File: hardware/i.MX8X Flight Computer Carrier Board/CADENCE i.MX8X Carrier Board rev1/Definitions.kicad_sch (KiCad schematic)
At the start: 8 parts, among them U41 TXS0101DCKR, U42 TXS0101DCKR, U45 TXS0108EPW

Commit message: schematic push
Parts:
- renumbered R159 to R160, R160 to R161, R163 to R162, U41 to U40, U42 to U41, U45 to U42
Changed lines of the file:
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@@
 		(on_board yes)
 		(dnp no)
-		(property "Reference" "#PWR0269"
+		(property "Reference" "#PWR0259"
 			(at 237.49 26.67 0)
 			(effects
@@
 			(project "CADENCE i.MX8X Carrier Board rev1"
 				(path "/de284495-d382-47cb-b528-76e440980d40/f5f49c98-aaea-4f03-a1b3-a277d1d06600/b523867a-62fb-4a81-ab53-06050067b1aa"
-					(reference "#PWR0269")
+					(reference "#PWR0259")
 					(unit 1)
 				)
@@
 		(on_board yes)
 		(dnp no)
-		(property "Reference" "#PWR0259"
+		(property "Reference" "#PWR0255"
 			(at 80.01 52.07 0)
 			(effects
@@
 			(project "CADENCE i.MX8X Carrier Board rev1"
 				(path "/de284495-d382-47cb-b528-76e440980d40/f5f49c98-aaea-4f03-a1b3-a277d1d06600/b523867a-62fb-4a81-ab53-06050067b1aa"
-					(reference "#PWR0259")
+					(reference "#PWR0255")
 					(unit 1)
 				)
@@
 		(on_board yes)
 		(dnp no)
-		(property "Reference" "#PWR0255"
+		(property "Reference" "#PWR0251"
 			(at 44.45 43.18 0)
 			(effects
@@
 			(project "CADENCE i.MX8X Carrier Board rev1"
 				(path "/de284495-d382-47cb-b528-76e440980d40/f5f49c98-aaea-4f03-a1b3-a277d1d06600/b523867a-62fb-4a81-ab53-06050067b1aa"
-					(reference "#PWR0255")
+					(reference "#PWR0251")
 					(unit 1)
 				)
@@
 		(on_board yes)
 		(dnp no)
-		(property "Reference" "#PWR0256"
+		(property "Reference" "#PWR0252"
 			(at 45.72 21.59 0)
 			(effects
@@
 			(project "CADENCE i.MX8X Carrier Board rev1"
 				(path "/de284495-d382-47cb-b528-76e440980d40/f5f49c98-aaea-4f03-a1b3-a277d1d06600/b523867a-62fb-4a81-ab53-06050067b1aa"
-					(reference "#PWR0256")
+					(reference "#PWR0252")
 					(unit 1)
 				)
@@
 		(on_board yes)
 		(dnp no)
-		(property "Reference" "#PWR0260"
+		(property "Reference" "#PWR0256"
 			(at 81.28 33.02 0)
 			(effects
@@
 			(project "CADENCE i.MX8X Carrier Board rev1"
 				(path "/de284495-d382-47cb-b528-76e440980d40/f5f49c98-aaea-4f03-a1b3-a277d1d06600/b523867a-62fb-4a81-ab53-06050067b1aa"
-					(reference "#PWR0260")
+					(reference "#PWR0256")
 					(unit 1)
 				)
@@
 		(on_board yes)
 		(dnp no)
-		(property "Reference" "#PWR0267"
+		(property "Reference" "#PWR0257"
 			(at 232.41 26.67 0)
 			(effects
@@
 			(project "CADENCE i.MX8X Carrier Board rev1"
 				(path "/de284495-d382-47cb-b528-76e440980d40/f5f49c98-aaea-4f03-a1b3-a277d1d06600/b523867a-62fb-4a81-ab53-06050067b1aa"
-					(reference "#PWR0267")
+					(reference "#PWR0257")
 					(unit 1)
 				)
@@
 		(on_board yes)
 		(dnp no)
-		(property "Reference" "R159"
+		(property "Reference" "R160"
 			(at 48.26 44.45 0)
 			(effects
@@
 			(project "CADENCE i.MX8X Carrier Board rev1"
 				(path "/de284495-d382-47cb-b528-76e440980d40/f5f49c98-aaea-4f03-a1b3-a277d1d06600/b523867a-62fb-4a81-ab53-06050067b1aa"
-					(reference "R159")
+					(reference "R160")
 					(unit 1)
 				)
@@
 		(on_board yes)
 		(dnp no)
-		(property "Reference" "R160"
+		(property "Reference" "R161"
 			(at 49.53 22.86 0)
 			(effects
@@
 			(project "CADENCE i.MX8X Carrier Board rev1"
 				(path "/de284495-d382-47cb-b528-76e440980d40/f5f49c98-aaea-4f03-a1b3-a277d1d06600/b523867a-62fb-4a81-ab53-06050067b1aa"
-					(reference "R160")
+					(reference "R161")
 					(unit 1)
 				)
@@
 		(on_board yes)
 		(dnp no)
-		(property "Reference" "U45"
+		(property "Reference" "U42"
 			(at 244.094 56.134 0)
 			(effects
@@
 			(project ""
 				(path "/de284495-d382-47cb-b528-76e440980d40/f5f49c98-aaea-4f03-a1b3-a277d1d06600/b523867a-62fb-4a81-ab53-06050067b1aa"
-					(reference "U45")
+					(reference "U42")
 					(unit 1)
 				)
@@
 		(on_board yes)
 		(dnp no)
-		(property "Reference" "#PWR0257"
+		(property "Reference" "#PWR0253"
 			(at 78.74 66.04 0)
 			(effects
@@
 			(project "CADENCE i.MX8X Carrier Board rev1"
 				(path "/de284495-d382-47cb-b528-76e440980d40/f5f49c98-aaea-4f03-a1b3-a277d1d06600/b523867a-62fb-4a81-ab53-06050067b1aa"
-					(reference "#PWR0257")
+					(reference "#PWR0253")
 					(unit 1)
 				)
@@
 		(on_board yes)
 		(dnp no)
-		(property "Reference" "U42"
+		(property "Reference" "U41"
 			(at 58.42 26.416 0)
 			(effects
@@
 			(project "CADENCE i.MX8X Carrier Board rev1"
 				(path "/de284495-d382-47cb-b528-76e440980d40/f5f49c98-aaea-4f03-a1b3-a277d1d06600/b523867a-62fb-4a81-ab53-06050067b1aa"
-					(reference "U42")
+					(reference "U41")
 					(unit 1)
 				)
@@
 		(on_board yes)
 		(dnp no)
-		(property "Reference" "U41"
+		(property "Reference" "U40"
 			(at 57.15 48.006 0)
 			(effects
@@
 			(project "CADENCE i.MX8X Carrier Board rev1"
 				(path "/de284495-d382-47cb-b528-76e440980d40/f5f49c98-aaea-4f03-a1b3-a277d1d06600/b523867a-62fb-4a81-ab53-06050067b1aa"
-					(reference "U41")
+					(reference "U40")
 					(unit 1)
 				)
@@
 		(on_board yes)
 		(dnp no)
-		(property "Reference" "R163"
+		(property "Reference" "R162"
 			(at 222.25 26.67 0)
 			(effects
@@
 			(project "CADENCE i.MX8X Carrier Board rev1"
 				(path "/de284495-d382-47cb-b528-76e440980d40/f5f49c98-aaea-4f03-a1b3-a277d1d06600/b523867a-62fb-4a81-ab53-06050067b1aa"
-					(reference "R163")
+					(reference "R162")
 					(unit 1)
 				)
@@
 		(on_board yes)
 		(dnp no)
-		(property "Reference" "#PWR0258"
+		(property "Reference" "#PWR0254"
 			(at 80.01 44.45 0)
 			(effects
@@
 			(project "CADENCE i.MX8X Carrier Board rev1"
 				(path "/de284495-d382-47cb-b528-76e440980d40/f5f49c98-aaea-4f03-a1b3-a277d1d06600/b523867a-62fb-4a81-ab53-06050067b1aa"
-					(reference "#PWR0258")
+					(reference "#PWR0254")
 					(unit 1)
 				)
@@
 		(on_board yes)
 		(dnp no)
-		(property "Reference" "#PWR0268"
+		(property "Reference" "#PWR0258"
 			(at 234.95 68.58 0)
 			(effects
@@
 			(project "CADENCE i.MX8X Carrier Board rev1"
 				(path "/de284495-d382-47cb-b528-76e440980d40/f5f49c98-aaea-4f03-a1b3-a277d1d06600/b523867a-62fb-4a81-ab53-06050067b1aa"
-					(reference "#PWR0268")
-					(unit 1)
-				)
+					(reference "#PWR0258")
+					(unit 1)
+				)

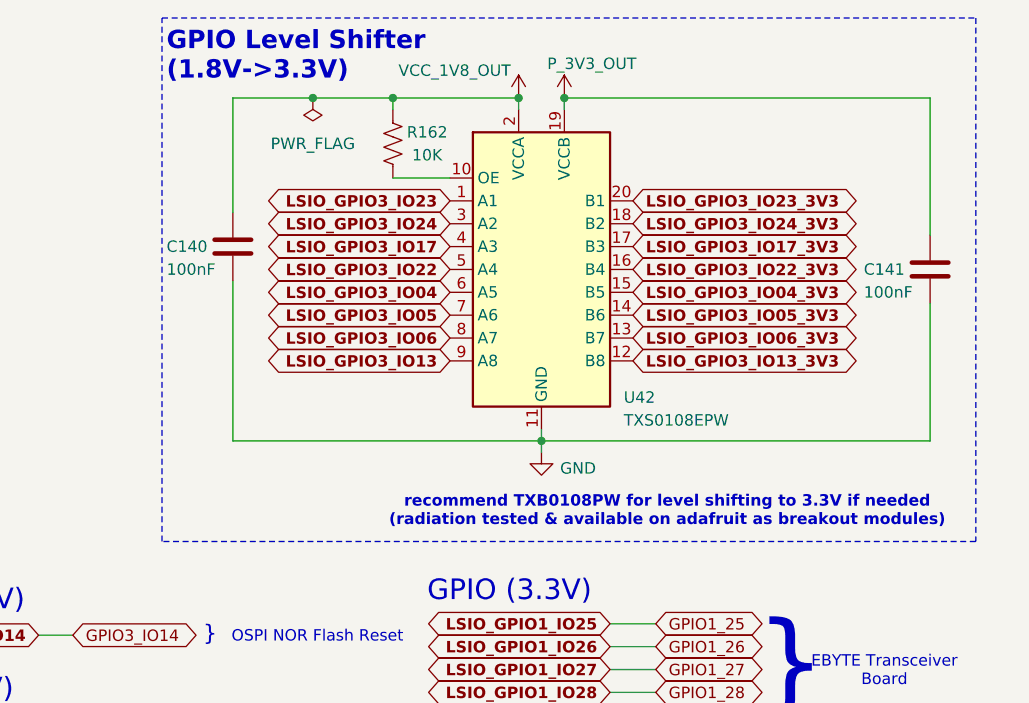
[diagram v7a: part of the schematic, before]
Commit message: removed most headers, few more connections
- added power headers
- removed many signal debug headers/gpio headers
ftdi usb connection
-jtag connection
- finishing up ethernet connections
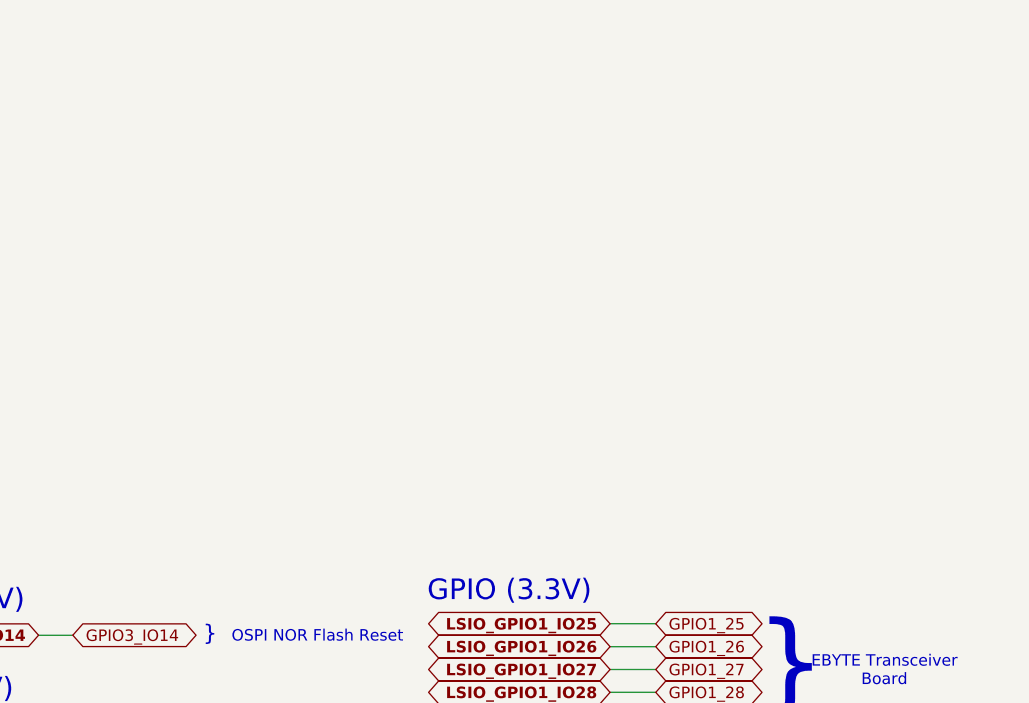
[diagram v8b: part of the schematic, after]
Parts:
- removed C140, C141: 100nF, Capacitor_SMD:C_0402_1005Metric, symbol Device:C
- removed R162: 10K, Resistor_SMD:R_0402_1005Metric, symbol Device:R_US
- removed U42: TXS0108EPW, Package_SO:TSSOP-20_4.4x6.5mm_P0.65mm, symbol Logic_LevelTranslator:TXS0108EPW
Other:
- note removed: "GPIO Level Shifter (1.8V->3.3V)"
- note removed: "recommend TXB0108PW for level shifting to 3.3V if needed (radiation tested & available on adafruit as breakout modules)"
